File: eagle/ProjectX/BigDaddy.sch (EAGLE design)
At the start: 180 parts, among them U10 TC4427AEOA, U11 TC4427AEOA, U12 TC4427AEOA, U13 TC4427AEOA, U19 TC4427AEOA, U20 TC4427AEOA, U21 TC4427AEOA, U22 TC4427AEOA, U23 TC4427AEOA, U24 TC4427AEOA, U25 TC4427AEOA, U26 TC4427AEOA, U27 TC4427AEOA, U28 TC4427AEOA, U29 TC4427AEOA, U3 TC4427AEOA, U30 TC4427AEOA, U31 TC4427AEOA, U32 TC4427AEOA, U34 TC4427AEOA, U35 TC4427AEOA, U36 TC4427AEOA, U37 TC4427AEOA, U38 TC4427AEOA, U39 TC4427AEOA, U4 TC4427AEOA, U40 TC4427AEOA, U41 TC4427AEOA, U42 TC4427AEOA, U43 TC4427AEOA, U44 TC4427AEOA, U45 TC4427AEOA, U5 TC4427AEOA, U55 TC4427AEOA, U56 TC4427AEOA, U57 TC4427AEOA, U58 TC4427AEOA, U59 TC4427AEOA, U60 TC4427AEOA, U61 TC4427AEOA, U62 TC4427AEOA, U63 TC4427AEOA, U7 TC4427AEOA, U9 TC4427AEOA

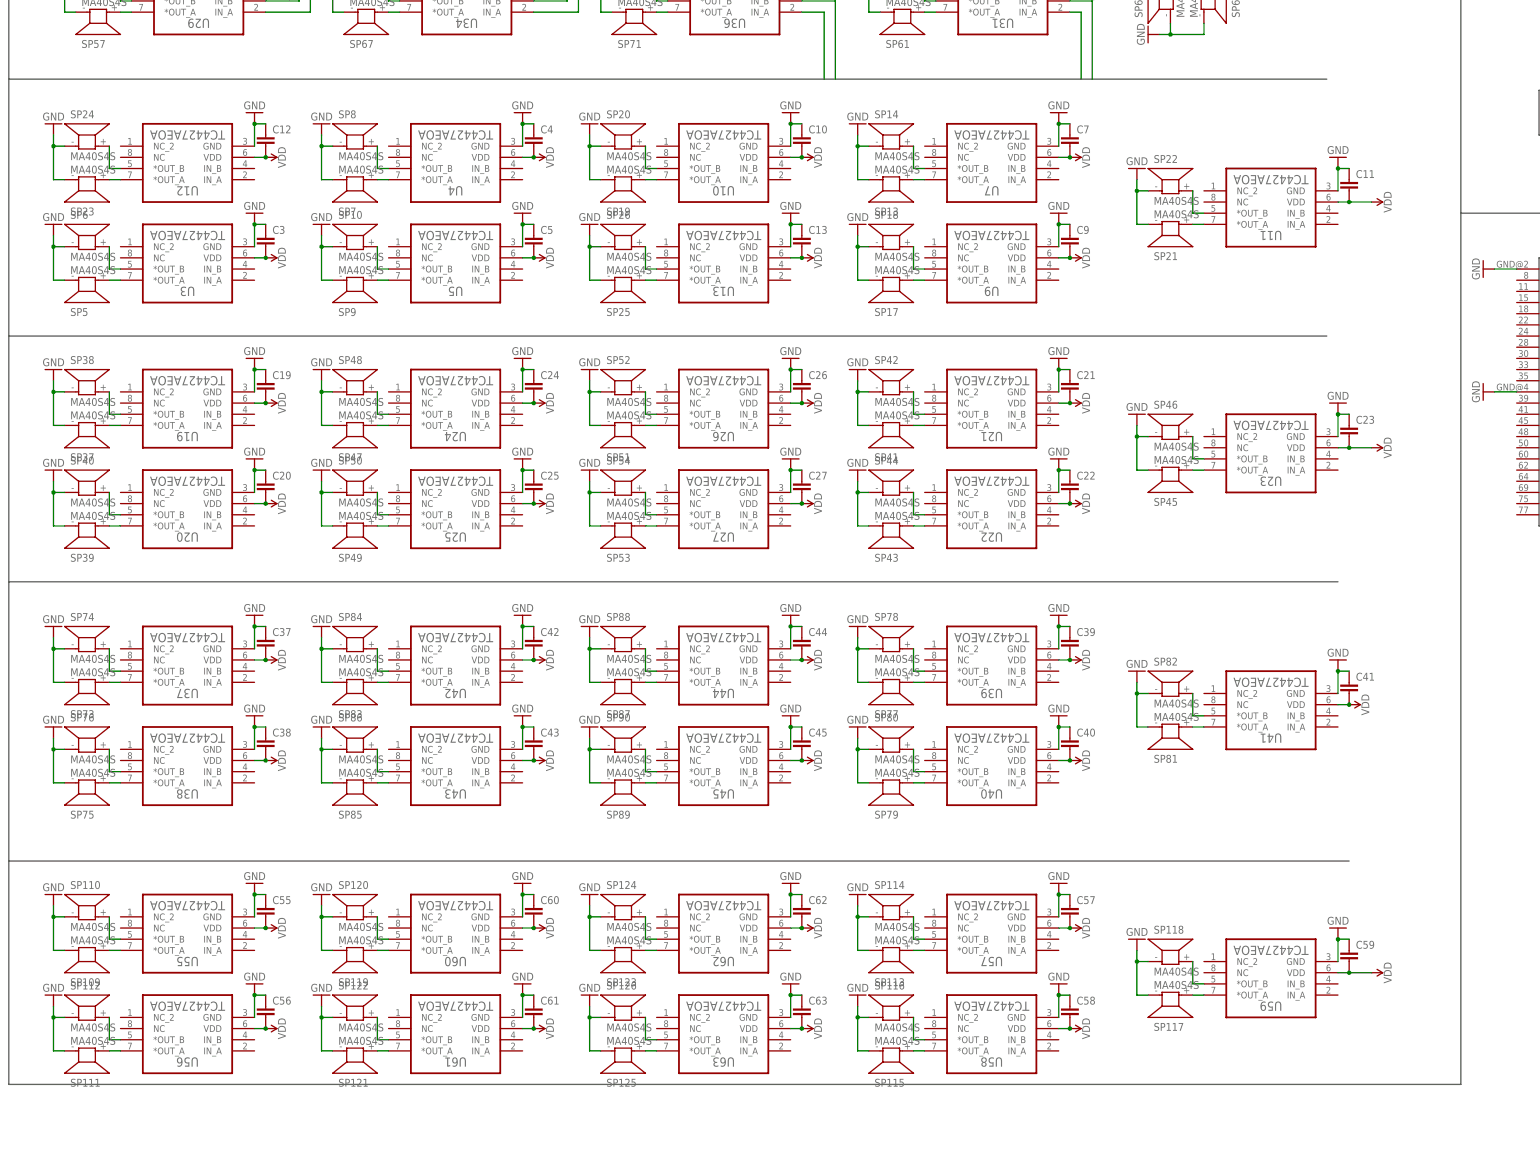
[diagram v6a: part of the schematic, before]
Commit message: Netted up all the remaining amplifiers, need to route and net the FPGA pins to the amplifiers
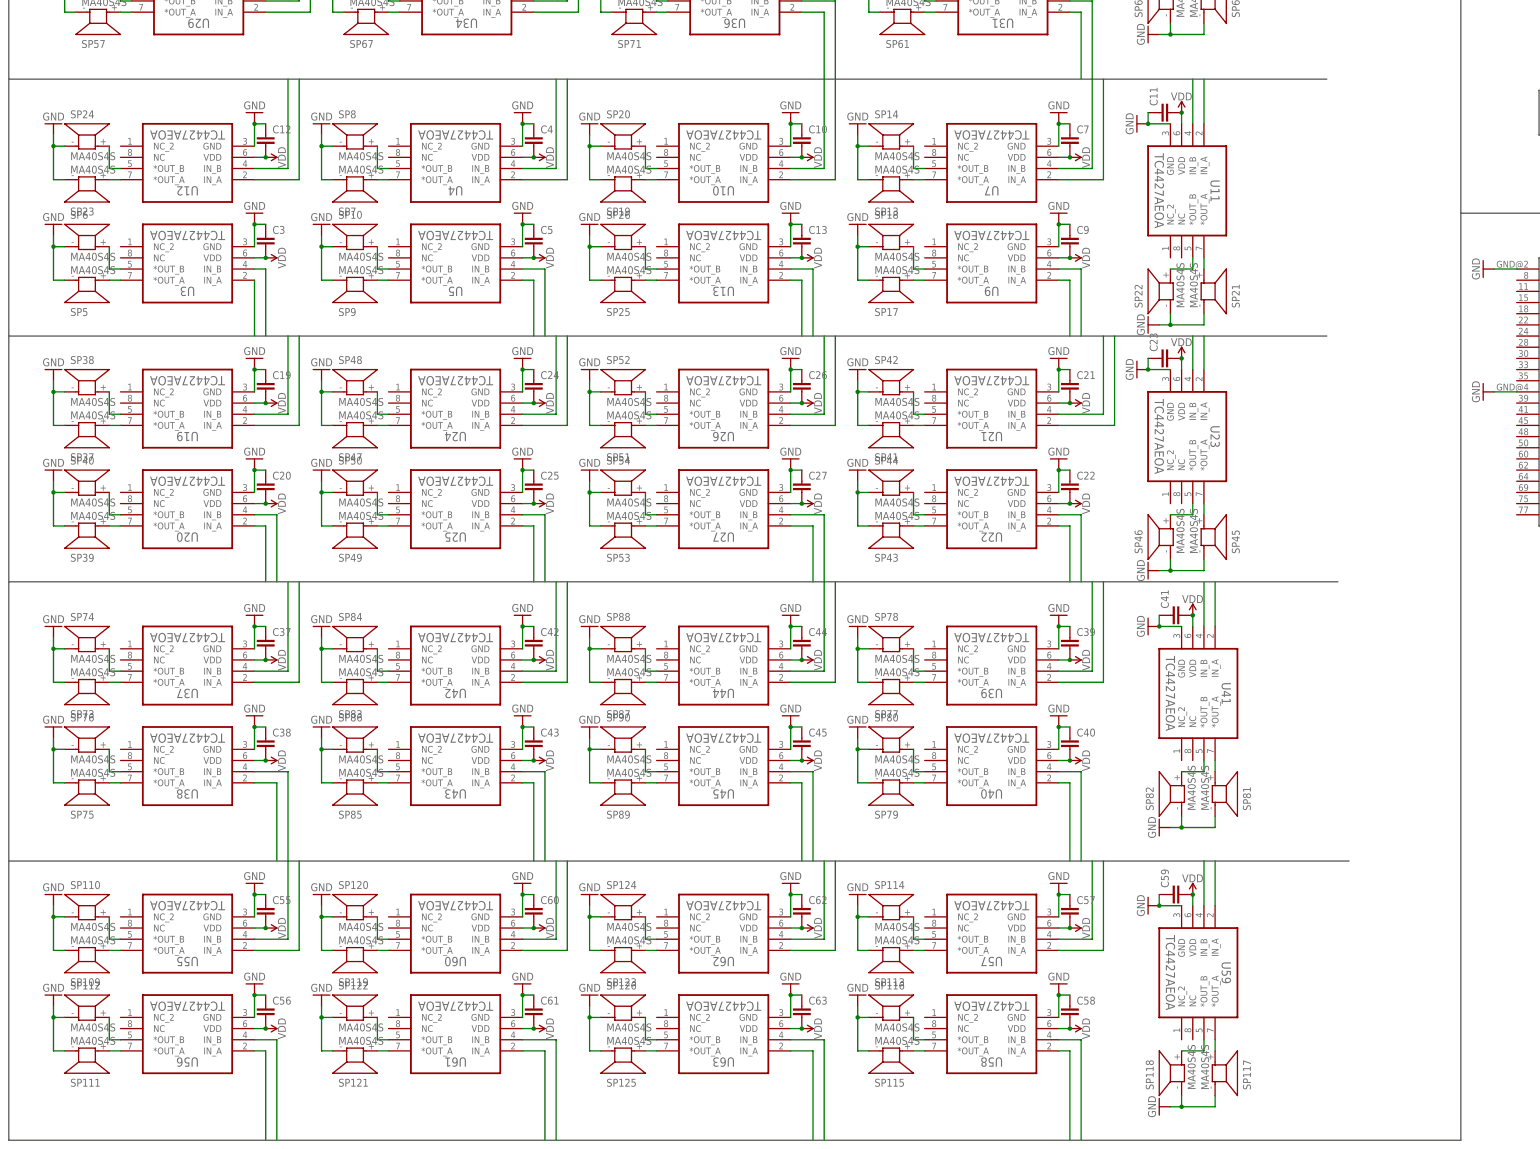
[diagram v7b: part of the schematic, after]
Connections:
- new net 17: U12.IN_B
- new net 18: U12.IN_A
- new net 19: U4.IN_B
- new net 20: U4.IN_A
- new net 21: U10.IN_B
- new net 22: U10.IN_A
- new net 23: U7.IN_B
- new net 24: U7.IN_A
- new net 25: U11.IN_A
- new net 26: U3.IN_B
- new net 27: U3.IN_A
- new net 28: U5.IN_B
- new net 29: U5.IN_A
- new net 30: U13.IN_B
- new net 31: U13.IN_A
- new net 32: U9.IN_B
- new net 33: U9.IN_A
- new net 34: U11.IN_B
- new net 35: U19.IN_B
- new net 36: U19.IN_A
- new net 37: U24.IN_B
- new net 38: U24.IN_A
- new net 39: U26.IN_B
- new net 40: U26.IN_A
- new net 41: U21.IN_B
- new net 42: U21.IN_A
- new net 43: U23.IN_A
- new net 44: U20.IN_B
- new net 45: U20.IN_A
- new net 46: U25.IN_B
- new net 47: U25.IN_A
- new net 48: U27.IN_B
- new net 49: U27.IN_A
- new net 50: U22.IN_B
- new net 51: U22.IN_A
- new net 52: U23.IN_B
- new net 53: U37.IN_B
- new net 54: U37.IN_A
- new net 55: U42.IN_B
- new net 56: U42.IN_A
- new net 57: U44.IN_B
- new net 58: U44.IN_A
- new net 59: U39.IN_B
- new net 60: U39.IN_A
- new net 61: U41.IN_A
- new net 62: U38.IN_B
- new net 63: U38.IN_A
- new net 64: U43.IN_B
- new net 65: U43.IN_A
- new net 66: U45.IN_B
- new net 67: U45.IN_A
- new net 68: U40.IN_B
- new net 69: U40.IN_A
- new net 70: U41.IN_B
- new net 71: U55.IN_B
- new net 72: U55.IN_A
- new net 73: U60.IN_B
- new net 74: U60.IN_A
- new net 75: U62.IN_B
- new net 76: U62.IN_A
- new net 77: U57.IN_B
- new net 78: U57.IN_A
- new net 79: U59.IN_A
- new net 80: U56.IN_B
- new net 81: U56.IN_A
- new net 82: U61.IN_B
- new net 83: U61.IN_A
- new net 84: U63.IN_B
- new net 85: U63.IN_A
- new net 86: U58.IN_B
- new net 87: U58.IN_A
- new net 88: U59.IN_B
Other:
- moved on the sheet: C11, C23, C41, C59, SP117, SP118, SP21, SP22, SP45, SP46, SP81, SP82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

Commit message: About 40% complete wiring of signals
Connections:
- net 10: now also DIP1.192; no longer DIP1.189
- net 11: now also DIP1.189; no longer DIP1.186
- net 17: now also DIP1.11
- net 18: now also DIP1.15
- net 19: now also DIP1.19
- net 20: now also DIP1.16
- net 21: now also DIP1.186
- net 22: now also DIP1.181
- net 26: now also DIP1.30
- net 27: now also DIP1.33
- net 28: now also DIP1.31
- net 29: now also DIP1.29
- net 35: now also DIP1.35
- net 36: now also DIP1.39
- net 37: now also DIP1.40
- net 38: now also DIP1.36
- net 44: now also DIP1.41
- net 45: now also DIP1.45
- net 46: now also DIP1.47
- net 47: now also DIP1.42
- net 53: now also DIP1.48
- net 54: now also DIP1.50
- net 55: now also DIP1.55
- net 56: now also DIP1.49
- net 62: now also DIP1.77
- net 63: now also DIP1.75
- net 64: now also DIP1.63
- net 65: now also DIP1.61
- net 71: now also DIP1.69
- net 72: now also DIP1.64
- net 73: now also DIP1.74
- net 74: now also DIP1.65
- net 80: now also DIP1.62
- net 81: now also DIP1.60
- net 82: now also DIP1.82
- net 83: now also DIP1.76
